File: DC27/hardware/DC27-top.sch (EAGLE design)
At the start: 34 parts, among them IC1 PCA9956BTWY, J1 top-bot-connector

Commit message: basic layout nearly done
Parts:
- removed J1: top-bot-connector, connector:M06SILK_FEMALE_PTH
- added C26, C27, C28, C29: 15 pF, passives:C-USC0805
- added D1, D2: DIODE-SCHOTTKYSOD-123FL, passives:DIODE-SCHOTTKYSOD-123FL
- added TOP-BOT-CONNECTOR: M06X2, connector:M06X2
- added U$11, U$12, U$13, U$14: APA1025050, leds:APA1025050
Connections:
- new net APA102_CLK: TOP-BOT-CONNECTOR.5, U$13.CI
- new net APA102_DATA: TOP-BOT-CONNECTOR.3, U$13.DI
- new net N$25: D2.C, U$3.3V3
- new net N$26: D1.C, U$4.3V3
- new net N$27: U$11.DI, U$12.DO
- new net N$28: U$11.GND, U$12.GND, U$13.GND, U$14.GND
- new net N$29: U$12.CI, U$14.CO
- new net N$34: U$11.CI, U$12.CO
- new net N$37: U$12.DI, U$14.DO
- new net N$38: U$13.DO, U$14.DI
- new net N$39: U$13.CO, U$14.CI
- new net VBAT: TOP-BOT-CONNECTOR.1
- net GND: now also C26.2, C27.2, C28.2, C29.2, TOP-BOT-CONNECTOR.11, TOP-BOT-CONNECTOR.12; no longer J1.6
- net GPIO1: now also TOP-BOT-CONNECTOR.8; no longer J1.4
- net GPIO2: now also TOP-BOT-CONNECTOR.10; no longer J1.5
- net SCL: now also TOP-BOT-CONNECTOR.4; no longer J1.2
- net SDA: now also TOP-BOT-CONNECTOR.6; no longer J1.3
- net VCC: now also C26.1, C27.1, C28.1, C29.1, D1.A, D2.A, TOP-BOT-CONNECTOR.2, U$11.VCC, U$12.VCC, U$13.VCC, U$14.VCC; no longer J1.1, U$3.3V3, U$4.3V3

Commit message: top board nearly complete
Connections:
- removed net N$28: U$11.GND, U$12.GND, U$13.GND, U$14.GND
- net GND: now also U$11.GND, U$12.GND, U$13.GND, U$14.GND
- net VBAT: now also C1.2, C26.1, C27.1, C28.1, C29.1, IC1.VDD, R2.1, U$11.VCC, U$12.VCC, U$13.VCC, U$14.VCC
- net VCC: no longer C1.2, C26.1, C27.1, C28.1, C29.1, IC1.VDD, R2.1, U$11.VCC, U$12.VCC, U$13.VCC, U$14.VCC

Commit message: what should be sent to pcbway
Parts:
- U$5: value DN_LOGODC26 -> DN_LOGO; device logos:DN_LOGODC26 -> logos:DN_LOGO
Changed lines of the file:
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@@
 <?xml version="1.0" encoding="utf-8"?>
 <!DOCTYPE eagle SYSTEM "eagle.dtd">
-<eagle version="9.3.0">
+<eagle version="9.3.2">
 <drawing>
 <settings>
-<setting alwaysvectorfont="no"/>
+<setting alwaysvectorfont="yes"/>
 <setting verticaltext="up"/>
 </settings>
 <grid distance="0.1" unitdist="inch" unit="inch" style="lines" multiple="1" display="no" altdistance="0.01" altunitdist="inch" altunit="inch"/>
 <layers>
-<layer number="1" name="Top" color="4" fill="1" visible="no" active="no"/>
-<layer number="2" name="Route2" color="16" fill="1" visible="no" active="no"/>
-<layer number="3" name="Route3" color="17" fill="1" visible="no" active="no"/>
-<layer number="4" name="Route4" color="18" fill="1" visible="no" active="no"/>
-<layer number="5" name="Route5" color="19" fill="1" visible="no" active="no"/>
-<layer number="6" name="Route6" color="25" fill="1" visible="no" active="no"/>
-<layer number="7" name="Route7" color="26" fill="1" visible="no" active="no"/>
-<layer number="8" name="Route8" color="27" fill="1" visible="no" active="no"/>
-<layer number="9" name="Route9" color="28" fill="1" visible="no" active="no"/>
-<layer number="10" name="Route10" color="29" fill="1" visible="no" active="no"/>
-<layer number="11" name="Route11" color="30" fill="1" visible="no" active="no"/>
-<layer number="12" name="Route12" color="20" fill="1" visible="no" active="no"/>
-<layer number="13" name="Route13" color="21" fill="1" visible="no" active="no"/>
-<layer number="14" name="Route14" color="22" fill="1" visible="no" active="no"/>
-<layer number="15" name="Route15" color="23" fill="1" visible="no" active="no"/>
-<layer number="16" name="Bottom" color="1" fill="1" visible="no" active="no"/>
-<layer number="17" name="Pads" color="2" fill="1" visible="no" active="no"/>
-<layer number="18" name="Vias" color="2" fill="1" visible="no" active="no"/>
-<layer number="19" name="Unrouted" color="6" fill="1" visible="no" active="no"/>
-<layer number="20" name="Dimension" color="24" fill="1" visible="no" active="no"/>
-<layer number="21" name="tPlace" color="7" fill="1" visible="no" active="no"/>
-<layer number="22" name="bPlace" color="7" fill="1" visible="no" active="no"/>
-<layer number="23" name="tOrigins" color="15" fill="1" visible="no" active="no"/>
-<layer number="24" name="bOrigins" color="15" fill="1" visible="no" active="no"/>
-<layer number="25" name="tNames" color="7" fill="1" visible="no" active="no"/>
-<layer number="26" name="bNames" color="7" fill="1" visible="no" active="no"/>
-<layer number="27" name="tValues" color="7" fill="1" visible="no" active="no"/>
-<layer number="28" name="bValues" color="7" fill="1" visible="no" active="no"/>
+<layer number="1" name="Top" color="4" fill="1" visible="yes" active="no"/>
+<layer number="2" name="Route2" color="16" fill="1" visible="yes" active="no"/>
+<layer number="3" name="Route3" color="17" fill="1" visible="yes" active="no"/>
+<layer number="4" name="Route4" color="18" fill="1" visible="yes" active="no"/>
+<layer number="5" name="Route5" color="19" fill="1" visible="yes" active="no"/>
+<layer number="6" name="Route6" color="25" fill="1" visible="yes" active="no"/>
+<layer number="7" name="Route7" color="26" fill="1" visible="yes" active="no"/>
+<layer number="8" name="Route8" color="27" fill="1" visible="yes" active="no"/>
+<layer number="9" name="Route9" color="28" fill="1" visible="yes" active="no"/>
+<layer number="10" name="Route10" color="29" fill="1" visible="yes" active="no"/>
+<layer number="11" name="Route11" color="30" fill="1" visible="yes" active="no"/>
+<layer number="12" name="Route12" color="20" fill="1" visible="yes" active="no"/>
+<layer number="13" name="Route13" color="21" fill="1" visible="yes" active="no"/>
+<layer number="14" name="Route14" color="22" fill="1" visible="yes" active="no"/>
+<layer number="15" name="Route15" color="23" fill="1" visible="yes" active="no"/>
+<layer number="16" name="Bottom" color="1" fill="1" visible="yes" active="no"/>
+<layer number="17" name="Pads" color="2" fill="1" visible="yes" active="no"/>
+<layer number="18" name="Vias" color="2" fill="1" visible="yes" active="no"/>
+<layer number="19" name="Unrouted" color="6" fill="1" visible="yes" active="no"/>
+<layer number="20" name="Dimension" color="24" fill="1" visible="yes" active="no"/>
+<layer number="21" name="tPlace" color="7" fill="1" visible="yes" active="no"/>
+<layer number="22" name="bPlace" color="7" fill="1" visible="yes" active="no"/>
+<layer number="23" name="tOrigins" color="15" fill="1" visible="yes" active="no"/>
+<layer number="24" name="bOrigins" color="15" fill="1" visible="yes" active="no"/>
+<layer number="25" name="tNames" color="7" fill="1" visible="yes" active="no"/>
+<layer number="26" name="bNames" color="7" fill="1" visible="yes" active="no"/>
+<layer number="27" name="tValues" color="7" fill="1" visible="yes" active="no"/>
+<layer number="28" name="bValues" color="7" fill="1" visible="yes" active="no"/>
 <layer number="29" name="tStop" color="7" fill="3" visible="no" active="no"/>
 <layer number="30" name="bStop" color="7" fill="6" visible="no" active="no"/>
@@
 <layer number="35" name="tGlue" color="7" fill="4" visible="no" active="no"/>
 <layer number="36" name="bGlue" color="7" fill="5" visible="no" active="no"/>
-<layer number="37" name="tTest" color="7" fill="1" visible="no" active="no"/>
-<layer number="38" name="bTest" color="7" fill="1" visible="no" active="no"/>
+<layer number="37" name="tTest" color="7" fill="1" visible="yes" active="no"/>
+<layer number="38" name="bTest" color="7" fill="1" visible="yes" active="no"/>
 <layer number="39" name="tKeepout" color="4" fill="11" visible="no" active="no"/>
 <layer number="40" name="bKeepout" color="1" fill="11" visible="no" active="no"/>
@@
 <layer number="44" name="Drills" color="7" fill="1" visible="no" active="no"/>
 <layer number="45" name="Holes" color="7" fill="1" visible="no" active="no"/>
-<layer number="46" name="Milling" color="3" fill="1" visible="no" active="no"/>
-<layer number="47" name="Measures" color="7" fill="1" visible="no" active="no"/>
-<layer number="48" name="Document" color="7" fill="1" visible="no" active="no"/>
-<layer number="49" name="Reference" color="7" fill="1" visible="no" active="no"/>
-<layer number="50" name="dxf" color="7" fill="1" visible="no" active="no"/>
-<layer number="51" name="tDocu" color="7" fill="1" visible="no" active="no"/>
-<layer number="52" name="bDocu" color="7" fill="1" visible="no" active="no"/>
-<layer number="53" name="tGND_GNDA" color="7" fill="9" visible="no" active="no"/>
-<layer number="54" name="bGND_GNDA" color="1" fill="9" visible="no" active="no"/>
-<layer number="56" name="wert" color="7" fill="1" visible="no" active="no"/>
-<layer number="57" name="tCAD" color="7" fill="1" visible="no" active="no"/>
-<layer number="59" name="tCarbon" color="7" fill="1" visible="no" active="no"/>
-<layer number="60" name="bCarbon" color="7" fill="1" visible="no" active="no"/>
+<layer number="46" name="Milling" color="3" fill="1" visible="yes" active="no"/>
+<layer number="47" name="Measures" color="7" fill="1" visible="yes" active="no"/>
+<layer number="48" name="Document" color="7" fill="1" visible="yes" active="no"/>
+<layer number="49" name="Reference" color="7" fill="1" visible="yes" active="no"/>
+<layer number="50" name="dxf" color="7" fill="1" visible="yes" active="no"/>
+<layer number="51" name="tDocu" color="7" fill="1" visible="yes" active="no"/>
+<layer number="52" name="bDocu" color="7" fill="1" visible="yes" active="no"/>
+<layer number="53" name="tGND_GNDA" color="7" fill="9" visible="yes" active="no"/>
+<layer number="54" name="bGND_GNDA" color="1" fill="9" visible="yes" active="no"/>
+<layer number="56" name="wert" color="7" fill="1" visible="yes" active="no"/>
+<layer number="57" name="tCAD" color="7" fill="1" visible="yes" active="no"/>
+<layer number="59" name="tCarbon" color="7" fill="1" visible="yes" active="no"/>
+<layer number="60" name="bCarbon" color="7" fill="1" visible="yes" active="no"/>
 <layer number="88" name="SimResults" color="9" fill="1" visible="yes" active="yes"/>
 <layer number="89" name="SimProbes" color="9" fill="1" visible="yes" active="yes"/>
@@
 <part name="LED23" library="leds" deviceset="LED" device="REVERSEMOUNT"/>
 <part name="LED24" library="leds" deviceset="LED" device="REVERSEMOUNT"/>
-<part name="U$5" library="logos" deviceset="DN_LOGO" device="DC26"/>
+<part name="U$5" library="logos" deviceset="DN_LOGO" device="" value="DN_LOGO"/>
 <part name="U$2" library="logos" deviceset="CMD_C0DE_LOGO" device=""/>
 <part name="D1" library="passives" deviceset="DIODE-SCHOTTKY" device="SOD-123FL"/>

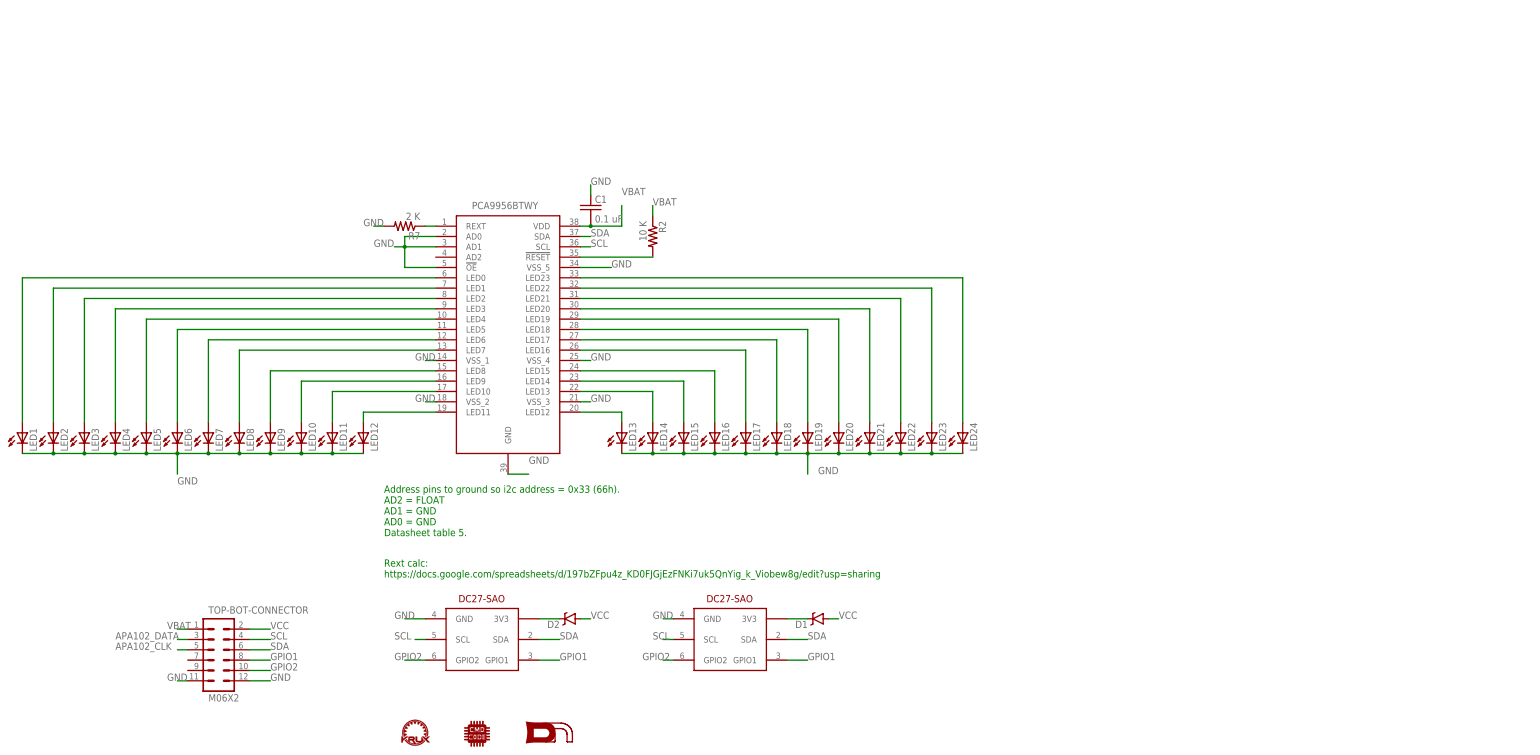
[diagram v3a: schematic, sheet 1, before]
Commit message: Fixed artwork
Fixed artwork which got mangled by Eagle's Push and shove routing
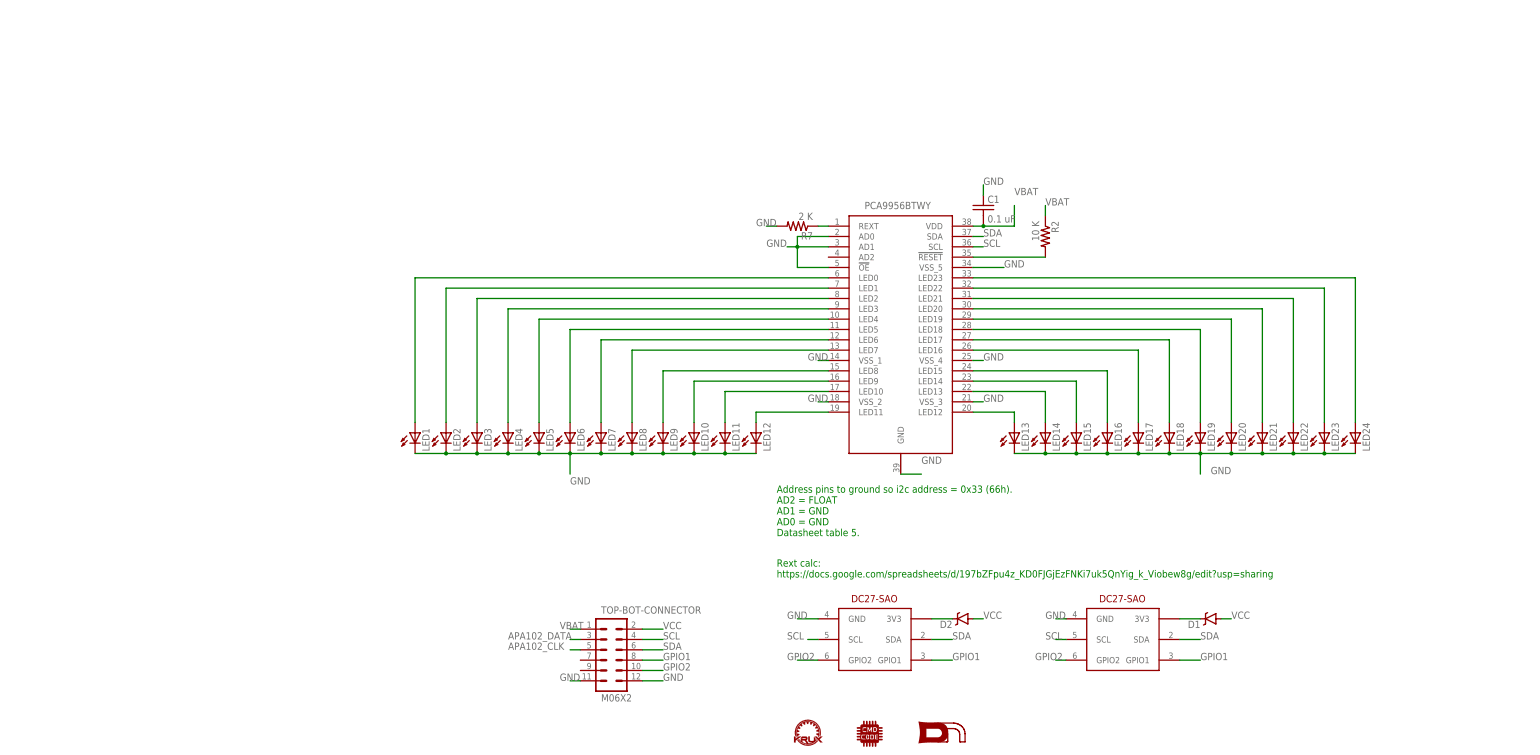
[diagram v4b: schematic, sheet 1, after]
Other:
- moved on the sheet: C1, D1, D2, LED1, LED10, LED11, LED12, LED13, LED14, LED15, LED16, LED17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

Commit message: removed apa 102s from top board swapped led driver for atmega4089 put on programming pads bottom board adding paring headers on bottom board added 1206 56 OHM resistors to each LED top board pulled out UPDI pin on top board for programming the atmega chip
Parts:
- removed C26, C27, C28, C29: 15 pF, passives:C-USC0805
- removed IC1: PCA9956BTWY, PCA9956BTWY:PCA9956BTWY
- removed U$11, U$12, U$13, U$14: APA1025050, leds:APA1025050
- added C2, C3: 0.1 uF, passives:C-USC0805
- added J1: (no value), connector:M04PTH
- added R1, R10, R11, R12, R13, R14, R15, R16, R17, R18, R19, R20, R21, R22, R23, R24, R3, R4, R5, R6, R8, R9: 56 R, passives:RESISTOR1206
- added U$6: ATMEGA4809-PFATMEL4809-PF, ICs:ATMEGA4809-PFATMEL4809-PF
- LED1, LED10, LED11, LED12, LED13, LED14, LED15, LED16, LED17, LED18, LED19, LED2, LED20, LED21, LED22, LED23, LED24, LED3, LED4, LED5, LED6, LED7, LED8, LED9: value (none) -> Amber
- R2: value 10 K -> 56 R; device darknet_parts_library:R-US_R0805 -> passives:RESISTOR1206
- R7: value 2 K -> 56 R; device darknet_parts_library:R-US_R0805 -> passives:RESISTOR1206
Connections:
- removed net APA102_CLK: TOP-BOT-CONNECTOR.5, U$13.CI
- removed net APA102_DATA: TOP-BOT-CONNECTOR.3, U$13.DI
- new net N$28: LED6.A, R6.1
- new net N$30: LED18.A, R18.2
- new net N$31: LED1.A, R1.1
- new net N$32: LED2.A, R2.1
- new net N$33: R17.1, U$6.PD5
- new net N$40: LED22.A, R22.1
- new net N$41: LED19.A, R19.1
- new net N$42: LED21.A, R21.1
- new net N$43: LED20.A, R20.1
- new net N$44: R19.2, U$6.PF5
- new net N$45: R20.2, U$6.PF2
- new net N$46: R21.2, U$6.PF1
- new net N$47: R22.2, U$6.PF0
- new net N$48: R23.2, U$6.PE3
- new net N$49: R24.2, U$6.PE2
- new net N$51: LED3.A, R3.2
- new net PA0: J1.4, U$6.PA0
- new net PC5: U$6.PC5
- new net PD1: U$6.PD1
- new net PD2: U$6.PD2
- new net PD3: U$6.PD3
- new net PF3: U$6.PF3
- new net PF4: U$6.PF4
- new net UPDI: J1.3, U$6.UPDI
- net GND: now also C2.1, C3.1, J1.2, U$6.GND0, U$6.GND2, U$6.GND3; no longer C26.2, C27.2, C28.2, C29.2, IC1.!OE, IC1.AD0, IC1.AD1, IC1.GND, IC1.VSS_1, IC1.VSS_2, IC1.VSS_3, IC1.VSS_4, IC1.VSS_5, R7.2, U$11.GND, U$12.GND, U$13.GND, U$14.GND
- net N$1: now also R9.2, U$6.PC3; no longer IC1.LED0, LED1.A
- net N$10: now also R10.1, U$6.PC2; no longer IC1.LED9, LED10.A
- net N$11: now also R11.2, U$6.PC1; no longer IC1.LED10, LED11.A
- net N$12: now also R12.2, U$6.PC0; no longer IC1.LED11, LED12.A
- net N$13: now also R4.2, U$6.PA4; no longer IC1.LED12, LED13.A
- net N$14: now also LED5.A, R5.1; no longer IC1.LED13, LED14.A
- net N$15: now also R5.2, U$6.PA1; no longer IC1.LED14, LED15.A
- net N$16: now also R13.1, U$6.PE1; no longer IC1.LED15, LED16.A
- net N$17: now also LED13.A, R13.2; no longer IC1.LED16, LED17.A
- net N$18: now also R14.1, U$6.PE0; no longer IC1.LED17, LED18.A
- net N$19: now also LED14.A, R14.2; no longer IC1.LED18, LED19.A
- net N$2: now also LED9.A, R9.1; no longer IC1.LED1, LED2.A
- net N$20: now also R15.1, U$6.PD7; no longer IC1.LED19, LED20.A
- net N$21: now also LED15.A, R15.2; no longer IC1.LED20, LED21.A
- net N$22: now also LED17.A, R17.2; no longer IC1.LED21, LED22.A
- net N$23: now also LED16.A, R16.2; no longer IC1.LED22, LED23.A
- net N$24: now also R18.1, U$6.PD4; no longer IC1.LED23, LED24.A
- net N$27: now also R6.2, U$6.PF6; no longer U$11.DI, U$12.DO
- net N$29: now also LED4.A, R4.1; no longer U$12.CI, U$14.CO
- net N$3: now also R8.2, U$6.PC4; no longer IC1.LED2, LED3.A
- net N$34: now also R16.1, U$6.PD6; no longer U$11.CI, U$12.CO
- net N$35: now also LED24.A, R24.1; no longer IC1.REXT, R7.1
- net N$36: now also LED10.A, R10.2; no longer IC1.!RESET, R2.2
- net N$37: now also LED11.A, R11.1; no longer U$12.DI, U$14.DO
- net N$38: now also LED12.A, R12.1; no longer U$13.DO, U$14.DI
- net N$39: now also LED23.A, R23.1; no longer U$13.CO, U$14.CI
- net N$4: now also R7.2, U$6.PD0; no longer IC1.LED3, LED4.A
- net N$5: now also R1.2, U$6.PA7; no longer IC1.LED4, LED5.A
- net N$6: now also R2.2, U$6.PA6; no longer IC1.LED5, LED6.A
- net N$7: now also R3.1, U$6.PA5; no longer IC1.LED6, LED7.A
- net N$8: now also R8.1; no longer IC1.LED7
- net N$9: now also LED7.A, R7.1; no longer IC1.LED8, LED9.A
- net SCL: now also U$6.PA3; no longer IC1.SCL
- net SDA: now also U$6.PA2; no longer IC1.SDA
- net VBAT: now also C2.2, C3.2, J1.1, U$6.AVDD, U$6.VDD0, U$6.VDD1; no longer C26.1, C27.1, C28.1, C29.1, IC1.VDD, R2.1, U$11.VCC, U$12.VCC, U$13.VCC, U$14.VCC
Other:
- note added: "https://www.elektormagazine.com/labs/arduino-for-updi-programming-for-atmega4809-and-tiny816817-with-jtag2updi https://github.com/ElTangas/jtag2updi"
- note removed: "Address pins to ground so i2c address = 0x33 (66h). AD2 = FLOAT AD1 = GND AD0 = GND Datasheet table 5."
- note removed: "Rext calc: https://docs.google.com/spreadsheets/d/197bZFpu4z_KD0FJGjEzFNKi7uk5QnYig_k_Viobew8g/edit?usp=sharing"

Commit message: Enable line of pwr switch is now what powers vbat on top board, so if you turnoff the badge top the top and the bottom board are off.  :) Increased top board caps to 1206 from 0805
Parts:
- added DOWN/RIGHT, UP/LEFT: SWITCH_TACTILETACTILE-2PIN-NARROW, switches:SWITCH_TACTILETACTILE-2PIN-NARROW
- C1, C2, C3: device passives:C-USC0805 -> passives:C-USC1206
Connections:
- new net SVN: TOP-BOT-CONNECTOR.3, UP/LEFT.A
- new net SVP: DOWN/RIGHT.A, TOP-BOT-CONNECTOR.5
- net GND: now also DOWN/RIGHT.C, UP/LEFT.C

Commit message: Fixed the darknet logo, and made resistors pretty
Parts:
- U$5: value DN_LOGO -> DN_LOGODC26; device logos:DN_LOGO -> darknet_parts_library:DN_LOGODC26
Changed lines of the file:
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@@
 <?xml version="1.0" encoding="utf-8"?>
 <!DOCTYPE eagle SYSTEM "eagle.dtd">
-<eagle version="9.4.1">
+<eagle version="9.4.0">
 <drawing>
 <settings>
-<setting alwaysvectorfont="yes"/>
+<setting alwaysvectorfont="no"/>
 <setting verticaltext="up"/>
 </settings>
@@
 <part name="LED23" library="leds" deviceset="LED" device="REVERSEMOUNT" value="Amber"/>
 <part name="LED24" library="leds" deviceset="LED" device="REVERSEMOUNT" value="Amber"/>
-<part name="U$5" library="logos" deviceset="DN_LOGO" device="" value="DN_LOGO"/>
+<part name="U$5" library="darknet_parts_library" deviceset="DN_LOGO" device="DC26" value="DN_LOGODC26"/>
 <part name="U$2" library="logos" deviceset="CMD_C0DE_LOGO" device=""/>
 <part name="D1" library="passives" deviceset="DIODE-SCHOTTKY" device="SOD-123FL"/>
